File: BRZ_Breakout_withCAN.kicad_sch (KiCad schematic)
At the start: 6 parts, among them J2 6376430-2, J3 6376430-2, J4 Conn_01x08_Socket, J5 Conn_01x08_Socket, J6 Conn_01x04_Socket, J7 Conn_01x10_Socket

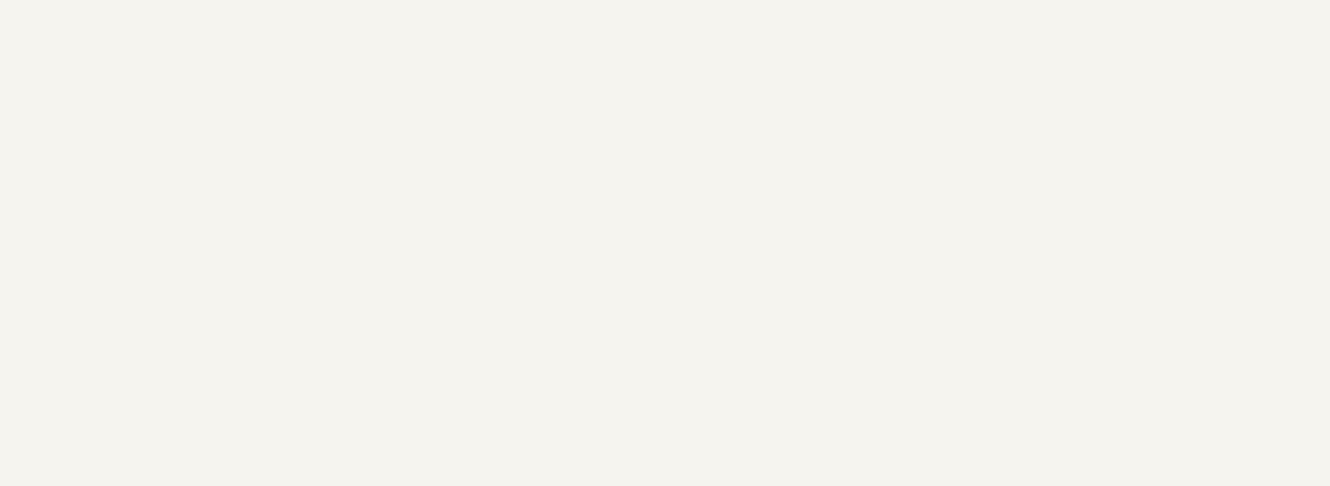
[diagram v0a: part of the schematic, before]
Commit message: Update Outline, Add breadboard area
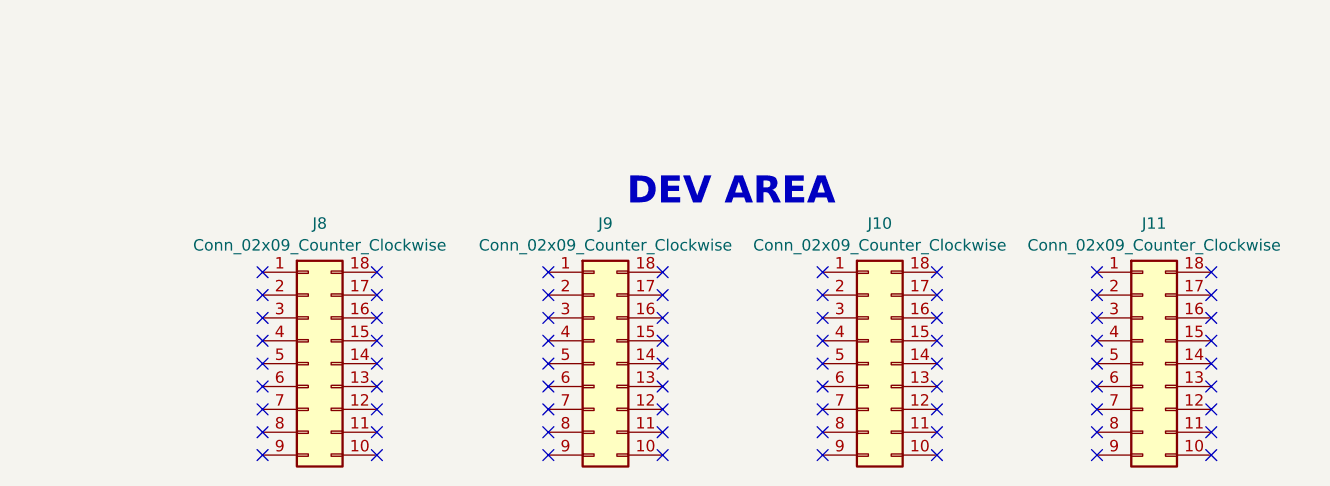
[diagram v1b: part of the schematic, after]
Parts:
- added J10, J11, J8, J9: Conn_02x09_Counter_Clockwise, Connector_PinHeader_2.54mm:PinHeader_2x09_P2.54mm_Vertical, symbol Connector_Generic:Conn_02x09_Counter_Clockwise
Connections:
- no-connect marks 0 -> 72
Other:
- note added: "DEV AREA"
